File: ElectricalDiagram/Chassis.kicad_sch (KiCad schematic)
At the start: 27 parts, among them J10 Conn_01x02, J11 Conn_01x02, J12 Conn_01x02, J13 Conn_01x02, J14 Conn_01x02, J15 Conn_01x08_Pin, J16 Conn_01x02, J17 Conn_01x02, J19 Conn_01x04_Pin, J20 Conn_01x04_Pin, J21 Conn_01x04_Pin, J22 Conn_01x02, J23 Conn_01x02, J24 Conn_01x04_Pin, J25 Conn_01x02, J26 Conn_01x02, J27 Conn_01x04_Pin, J28 Conn_01x04_Pin, J29 Conn_01x02, J3 Conn_01x02, J30 Conn_01x02, J4 Conn_01x02, J5 Conn_01x02, J6 Conn_01x02, J7 Conn_01x02, J8 Conn_01x02, J9 Conn_01x02

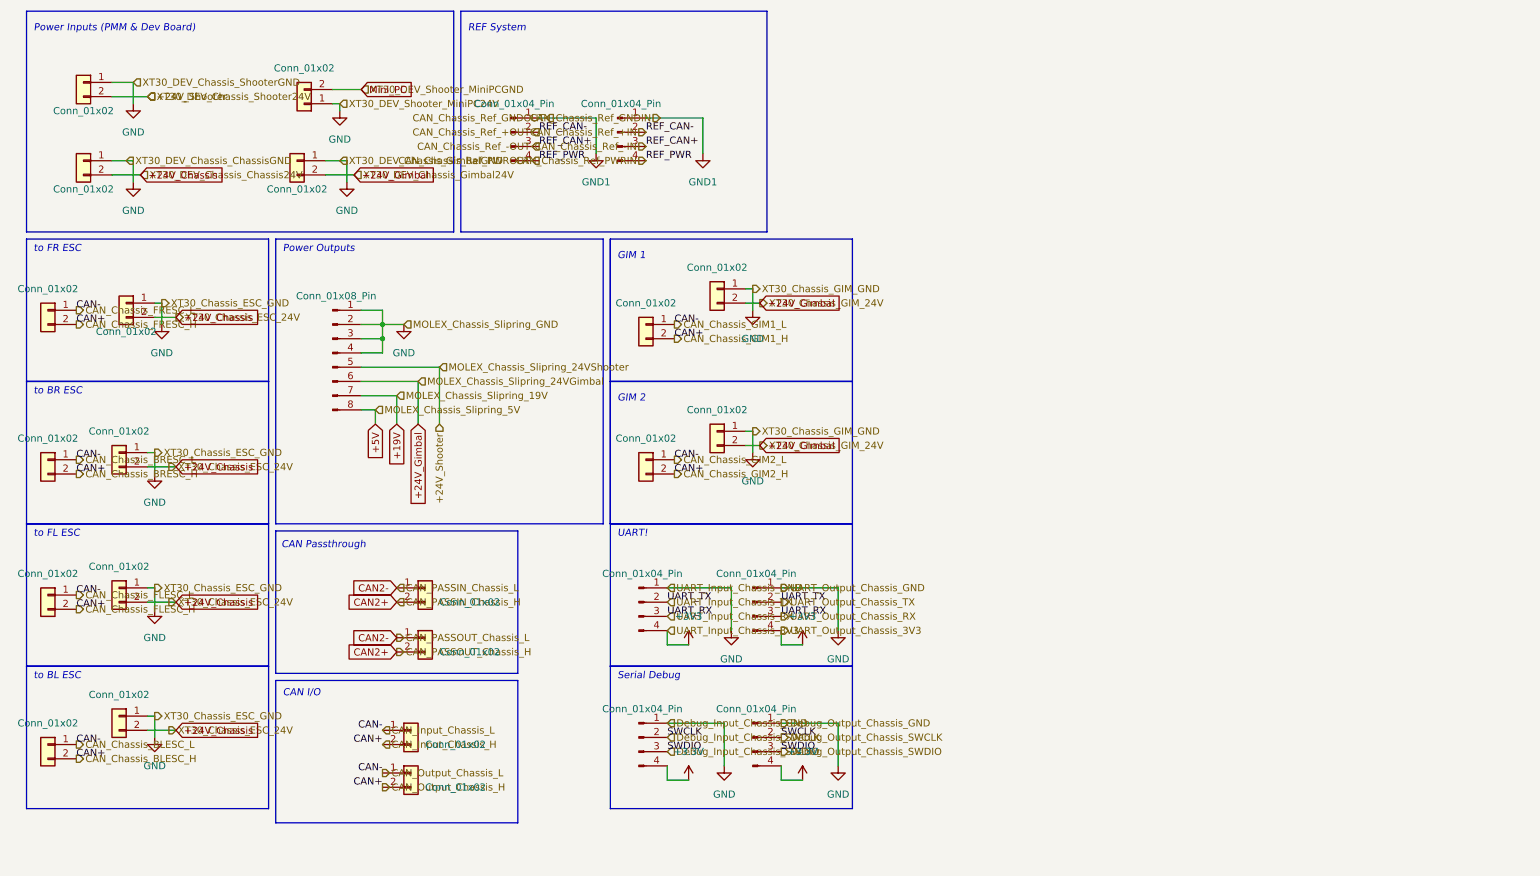
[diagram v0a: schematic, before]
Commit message: Staged hierarchical changes for chassis, not finished
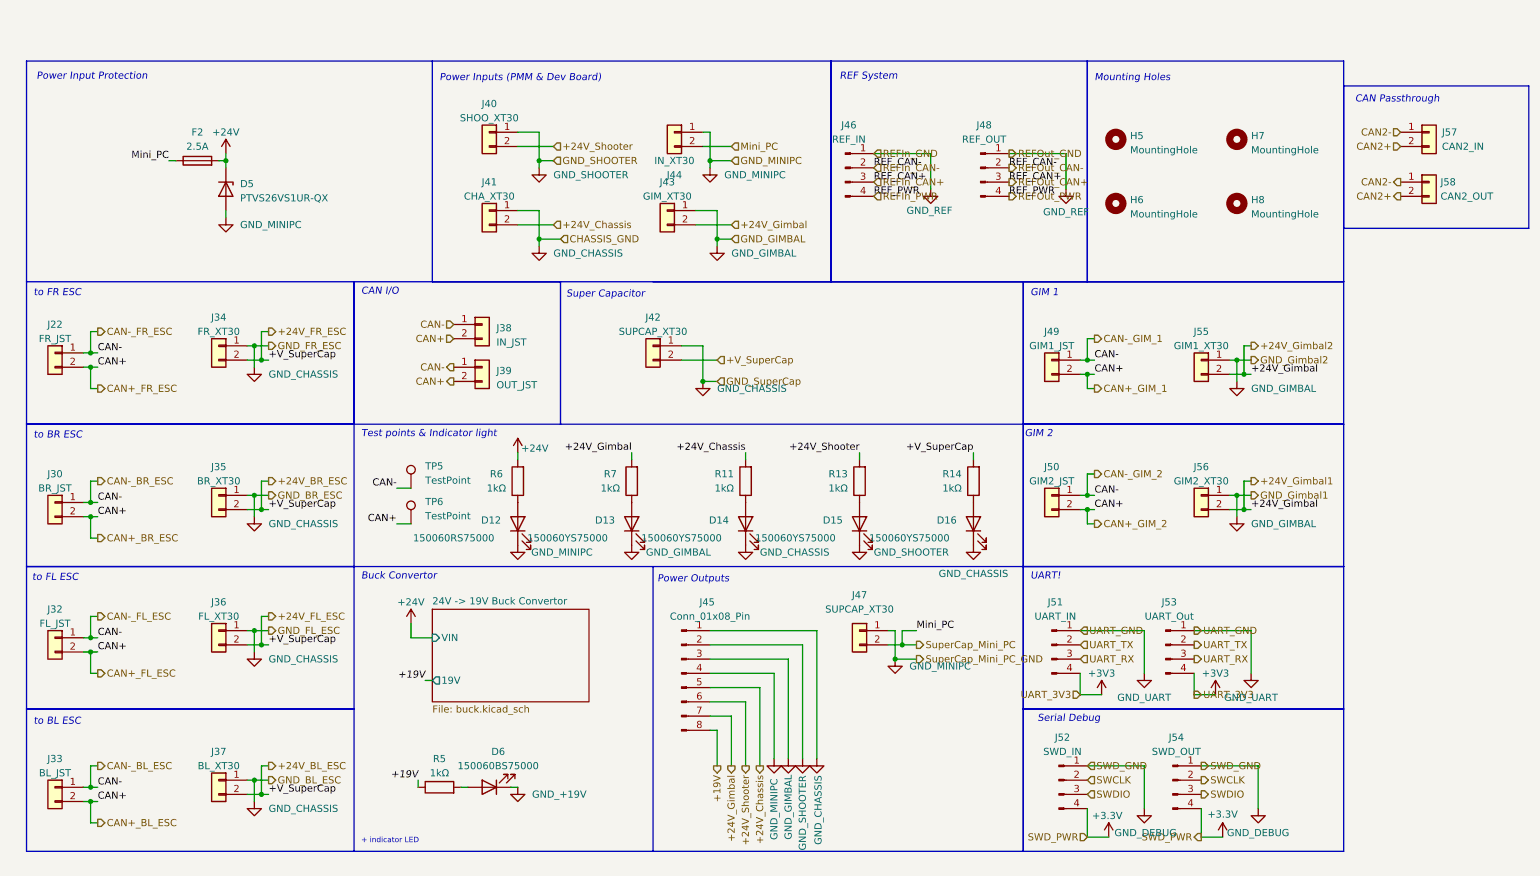
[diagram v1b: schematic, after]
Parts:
- removed J10, J11, J12, J13, J14, J16, J17, J23, J25, J26, J29, J3, J4, J5, J6, J7, J8, J9: Conn_01x02, symbol Connector_Generic:Conn_01x02
- removed J15: Conn_01x08_Pin, symbol Connector:Conn_01x08_Pin
- removed J19, J20, J21, J24, J27, J28: Conn_01x04_Pin, symbol Connector:Conn_01x04_Pin
- added D12: 150060RS75000, LED_SMD:LED_0603_1608Metric_Pad1.05x0.95mm_HandSolder, symbol Device:LED
- added D13, D14, D15, D16: 150060YS75000, LED_SMD:LED_0603_1608Metric_Pad1.05x0.95mm_HandSolder, symbol Device:LED
- added D5: PTVS26VS1UR-QX, Robomaster_Passives:PTVS26VS1URQX, symbol Device:D_Zener
- added D6: 150060BS75000, LED_SMD:LED_0603_1608Metric_Pad1.05x0.95mm_HandSolder, symbol Device:LED
- added F2: 2.5A, Fuse:Fuse_0603_1608Metric_Pad1.05x0.95mm_HandSolder, symbol Device:Fuse
- added H5, H6, H7, H8: MountingHole, MountingHole:MountingHole_3.2mm_M3, symbol Mechanical:MountingHole
- added J32: FL_JST, Connector_JST:JST_GH_BM02B-GHS-TBT_1x02-1MP_P1.25mm_Vertical, symbol Connector_Generic:Conn_01x02
- added J33: BL_JST, Connector_JST:JST_GH_BM02B-GHS-TBT_1x02-1MP_P1.25mm_Vertical, symbol Connector_Generic:Conn_01x02
- added J34: FR_XT30, Robomaster_Connectors:AMASS_XT30U-F_1x02_P5.0mm_Vertical, symbol Connector_Generic:Conn_01x02
- added J35: BR_XT30, Robomaster_Connectors:AMASS_XT30U-F_1x02_P5.0mm_Vertical, symbol Connector_Generic:Conn_01x02
- added J36: FL_XT30, Robomaster_Connectors:AMASS_XT30U-F_1x02_P5.0mm_Vertical, symbol Connector_Generic:Conn_01x02
- added J37: BL_XT30, Robomaster_Connectors:AMASS_XT30U-F_1x02_P5.0mm_Vertical, symbol Connector_Generic:Conn_01x02
- added J38: IN_JST, Connector_JST:JST_GH_BM02B-GHS-TBT_1x02-1MP_P1.25mm_Vertical, symbol Connector_Generic:Conn_01x02
- added J39: OUT_JST, Connector_JST:JST_GH_BM02B-GHS-TBT_1x02-1MP_P1.25mm_Vertical, symbol Connector_Generic:Conn_01x02
- added J40: SHOO_XT30, Robomaster_Connectors:AMASS_XT30U-F_1x02_P5.0mm_Vertical, symbol Connector_Generic:Conn_01x02
- added J41: CHA_XT30, Robomaster_Connectors:AMASS_XT30U-F_1x02_P5.0mm_Vertical, symbol Connector_Generic:Conn_01x02
- added J42, J47: SUPCAP_XT30, Robomaster_Connectors:AMASS_XT30U-F_1x02_P5.0mm_Vertical, symbol Connector_Generic:Conn_01x02
- added J43: GIM_XT30, Robomaster_Connectors:AMASS_XT30U-F_1x02_P5.0mm_Vertical, symbol Connector_Generic:Conn_01x02
- added J44: IN_XT30, Robomaster_Connectors:AMASS_XT30U-F_1x02_P5.0mm_Vertical, symbol Connector_Generic:Conn_01x02
- added J45: Conn_01x08_Pin, Robomaster_Connectors:CON_1722981108_MOL, symbol Connector:Conn_01x08_Pin
- added J46: REF_IN, Connector_JST:JST_GH_BM04B-GHS-TBT_1x04-1MP_P1.25mm_Vertical, symbol Connector:Conn_01x04_Pin
- added J48: REF_OUT, Connector_JST:JST_GH_BM04B-GHS-TBT_1x04-1MP_P1.25mm_Vertical, symbol Connector:Conn_01x04_Pin
- added J49: GIM1_JST, Connector_JST:JST_GH_BM02B-GHS-TBT_1x02-1MP_P1.25mm_Vertical, symbol Connector_Generic:Conn_01x02
- added J50: GIM2_JST, Connector_JST:JST_GH_BM02B-GHS-TBT_1x02-1MP_P1.25mm_Vertical, symbol Connector_Generic:Conn_01x02
- added J51: UART_IN, Connector_JST:JST_GH_BM04B-GHS-TBT_1x04-1MP_P1.25mm_Vertical, symbol Connector:Conn_01x04_Pin
- added J52: SWD_IN, Connector_JST:JST_GH_BM04B-GHS-TBT_1x04-1MP_P1.25mm_Vertical, symbol Connector:Conn_01x04_Pin
- added J53: UART_Out, Connector_JST:JST_GH_BM04B-GHS-TBT_1x04-1MP_P1.25mm_Vertical, symbol Connector:Conn_01x04_Pin
- added J54: SWD_OUT, Connector_JST:JST_GH_BM04B-GHS-TBT_1x04-1MP_P1.25mm_Vertical, symbol Connector:Conn_01x04_Pin
- added J55: GIM1_XT30, Robomaster_Connectors:AMASS_XT30U-F_1x02_P5.0mm_Vertical, symbol Connector_Generic:Conn_01x02
- added J56: GIM2_XT30, Robomaster_Connectors:AMASS_XT30U-F_1x02_P5.0mm_Vertical, symbol Connector_Generic:Conn_01x02
- added J57: CAN2_IN, Connector_JST:JST_GH_BM02B-GHS-TBT_1x02-1MP_P1.25mm_Vertical, symbol Connector_Generic:Conn_01x02
- added J58: CAN2_OUT, Connector_JST:JST_GH_BM02B-GHS-TBT_1x02-1MP_P1.25mm_Vertical, symbol Connector_Generic:Conn_01x02
- added R11, R13, R14, R5, R6, R7: 1kΩ, Resistor_SMD:R_0603_1608Metric_Pad0.98x0.95mm_HandSolder, symbol Device:R
- added TP5, TP6: TestPoint, TestPoint:TestPoint_Pad_2.0x2.0mm, symbol Connector:TestPoint
- J22: value Conn_01x02 -> FR_JST; footprint (none) -> Connector_JST:JST_GH_BM02B-GHS-TBT_1x02-1MP_P1.25mm_Vertical; Manufacturer_Part_Number (none) -> JST 2-pin
- J30: value Conn_01x02 -> BR_JST; footprint (none) -> Connector_JST:JST_GH_BM02B-GHS-TBT_1x02-1MP_P1.25mm_Vertical; Manufacturer_Part_Number (none) -> JST 2-pin
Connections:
- net +19V: now also J45.8 (Pin_8), R5.1
- net +24V_Chassis: now also J41.2 (Pin_2), J45.5 (Pin_5), R11.2
- net +24V_Gimbal: now also J43.2 (Pin_2), J45.7 (Pin_7), J55.2 (Pin_2), J56.2 (Pin_2), R7.2
- net +24V_Shooter: now also J40.2 (Pin_2), J45.6 (Pin_6), R13.2
- net +3.3V: now also J52.4 (Pin_4), J54.4 (Pin_4)
- net +3V3: now also J51.4 (Pin_4), J53.4 (Pin_4)
- net CAN2+: now also J57.2 (Pin_2), J58.2 (Pin_2); no longer J30.2 (Pin_2)
- net CAN2-: now also J57.1 (Pin_1), J58.1 (Pin_1); no longer J30.1 (Pin_1)
- net Mini_PC: now also F2.1, J44.2 (Pin_2), J47.2 (Pin_2)
- net CAN_Chassis_BLESC_H renamed CAN+
- net CAN+: now also J30.2 (Pin_2), J32.2 (Pin_2), J33.2 (Pin_2), J38.2 (Pin_2), J39.2 (Pin_2), J49.2 (Pin_2), J50.2 (Pin_2), TP6.1
- net CAN_Chassis_BLESC_L renamed CAN-
- net CAN-: now also J30.1 (Pin_1), J32.1 (Pin_1), J33.1 (Pin_1), J38.1 (Pin_1), J39.1 (Pin_1), J49.1 (Pin_1), J50.1 (Pin_1), TP5.1
- new net: D16.2 (A), R14.1
- new net: D15.2 (A), R13.1
- new net: D13.2 (A), R7.1
- new net: D12.2 (A), R6.1
- new net: D14.2 (A), R11.1
- new net: D6.2 (A), R5.2
- new net +24V: D5.1 (K), F2.2, R6.2
- new net +24V_BL_ESC: J34.2 (Pin_2), J35.2 (Pin_2), J36.2 (Pin_2), J37.2 (Pin_2), J42.2 (Pin_2), R14.2
- new net GND_+19V: D6.1 (K)
- new net GND_CHASSIS: D14.1 (K), D16.1 (K), J34.1 (Pin_1), J35.1 (Pin_1), J36.1 (Pin_1), J37.1 (Pin_1), J41.1 (Pin_1), J42.1 (Pin_1), J45.1 (Pin_1)
- new net GND_DEBUG: J52.1 (Pin_1), J54.1 (Pin_1)
- new net GND_GIMBAL: D13.1 (K), J43.1 (Pin_1), J45.3 (Pin_3), J55.1 (Pin_1), J56.1 (Pin_1)
- new net GND_MINIPC: D12.1 (K), D5.2 (A), J44.1 (Pin_1), J45.4 (Pin_4), J47.1 (Pin_1)
- new net GND_REF: J46.1 (Pin_1), J48.1 (Pin_1)
- new net GND_SHOOTER: D15.1 (K), J40.1 (Pin_1), J45.2 (Pin_2)
- new net GND_UART: J51.1 (Pin_1), J53.1 (Pin_1)
- new net REFIn_CAN+: J46.3 (Pin_3), J48.3 (Pin_3)
- new net REFIn_CAN-: J46.2 (Pin_2), J48.2 (Pin_2)
- new net REFIn_PWR: J46.4 (Pin_4), J48.4 (Pin_4)
- new net SWCLK: J52.2 (Pin_2), J54.2 (Pin_2)
- new net SWDIO: J52.3 (Pin_3), J54.3 (Pin_3)
- new net UART_RX: J51.3 (Pin_3), J53.3 (Pin_3)
- new net UART_TX: J51.2 (Pin_2), J53.2 (Pin_2)
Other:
- added sheet 24V -> 19V Buck Convertor (buck.kicad_sch)
- note added: "+ indicator LED"
- note added: "Buck Convertor"
- note added: "Mounting Holes"
- note added: "Power Input Protection"
- note added: "Super Capacitor"
- note added: "Test points & Indicator light"
- company: (none) -> UT RoboMasters
- title: (none) -> Chassis

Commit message: staging before meeting
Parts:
- renumbered D6 to D1, D5 to D10, D16 to D11, D12 to D2, D13 to D7, D14 to D8, D15 to D9, F2 to F1, H5 to H1, H6 to H2, H7 to H3, H8 to H4, J22 to J1, J44 to J10, J52 to J11, J47 to J12, J49 to J13, J50 to J14, J55 to J15, J56 to J16, J54 to J17, J41 to J18, J40 to J19, J30 to J2, J43 to J20, J39 to J21, J51 to J23, J53 to J24, J46 to J25, J48 to J26, J57 to J27, J58 to J28, J42 to J29, J32 to J3, J45 to J31, J33 to J4, J34 to J5, J35 to J6, J36 to J7, J37 to J8, J38 to J9, R5 to R1, R13 to R10, R14 to R12, R6 to R2, R7 to R8, R11 to R9, TP5 to TP1, TP6 to TP2
